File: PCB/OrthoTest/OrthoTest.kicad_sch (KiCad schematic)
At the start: 121 parts, among them SW1 SW_Push, SW10 SW_Push, SW11 SW_Push, SW12 SW_Push, SW13 SW_Push, SW14 SW_Push, SW15 SW_Push, SW16 SW_Push, SW17 SW_Push, SW18 SW_Push, SW19 SW_Push, SW2 SW_Push, SW20 SW_Push, SW21 SW_Push, SW22 SW_Push, SW23 SW_Push, SW24 SW_Push, SW25 SW_Push, SW26 SW_Push, SW27 SW_Push, SW28 SW_Push, SW29 SW_Push, SW3 SW_Push, SW30 SW_Push, SW31 SW_Push, SW32 SW_Push, SW33 SW_Push, SW34 SW_Push, SW35 SW_Push, SW36 SW_Push, SW37 SW_Push, SW38 SW_Push, SW39 SW_Push, SW4 SW_Push, SW40 SW_Push, SW41 SW_Push, SW42 SW_Push, SW43 SW_Push, SW44 SW_Push, SW45 SW_Push, SW46 SW_Push, SW47 SW_Push, SW48 SW_Push, SW49 SW_Push, SW5 SW_Push, SW50 SW_Push, SW51 SW_Push, SW52 SW_Push, SW53 SW_Push, SW54 SW_Push, SW55 SW_Push, SW56 SW_Push, SW57 SW_Push, SW58 SW_Push, SW59 SW_Push, SW6 SW_Push, SW60 SW_Push, SW7 SW_Push, SW8 SW_Push, SW9 SW_Push

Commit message: worked on it a lil
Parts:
- removed SW60: SW_Push, MyKeebLib:SW_Redragon_LowProfile_PCB_1.00u, symbol Switch:SW_Push
- added S1: MX_stab, PCM_marbastlib-mx:STAB_MX_2u, symbol PCM_marbastlib-mx:MX_stab
- added SW60, SW61: RotaryEncoder_Switch_MP, Rotary_Encoder:RotaryEncoder_Alps_EC11E-Switch_Vertical_H20mm, symbol Device:RotaryEncoder_Switch_MP
- added U1: ~, MyKeebLib:SSD1306-0.91-OLED-4pin-128x32, symbol MySymbols:ssd1306
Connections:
- net row1: now reaches D13.1 (K), D14.1 (K), D15.1 (K), D16.1 (K), D17.1 (K), D18.1 (K), D19.1 (K), D20.1 (K), D21.1 (K), D22.1 (K), D23.1 (K), D24.1 (K)
- net row2: now reaches D25.1 (K), D26.1 (K), D27.1 (K), D28.1 (K), D29.1 (K), D30.1 (K), D31.1 (K), D32.1 (K), D33.1 (K), D34.1 (K), D35.1 (K), D36.1 (K)
- net row0: now reaches D1.1 (K), D10.1 (K), D11.1 (K), D12.1 (K), D2.1 (K), D3.1 (K), D4.1 (K), D5.1 (K), D6.1 (K), D7.1 (K), D8.1 (K), D9.1 (K)
- net col10: now reaches SW47.1
- net col10: now also SW11.1, SW23.1, SW35.1, SW58.1
- net row3: now reaches D37.1 (K), D38.1 (K), D39.1 (K), D40.1 (K), D41.1 (K), D42.1 (K), D43.1 (K), D44.1 (K), D45.1 (K), D46.1 (K), D47.1 (K), D48.1 (K)
- net col2: now reaches SW3.1
- net col2: now also SW15.1, SW27.1, SW39.1, SW51.1
- net col0: now reaches SW25.1
- net col0: now also SW1.1, SW13.1, SW37.1, SW49.1
- net col7: now reaches SW8.1
- net col7: now also SW20.1, SW32.1, SW44.1, SW55.1
- net col1: now reaches SW50.1
- net col1: now also SW14.1, SW2.1, SW26.1, SW38.1
- net col5: now reaches SW30.1
- net col5: now also SW18.1, SW42.1, SW54.1, SW6.1
- net col4: now reaches SW41.1
- net col4: now also SW17.1, SW29.1, SW5.1, SW53.1
- net row4: now reaches D49.1 (K), D50.1 (K), D51.1 (K), D52.1 (K), D53.1 (K), D54.1 (K), D55.1 (K), D56.1 (K), D57.1 (K), D58.1 (K), D59.1 (K)
- net row4: no longer D60.1 (K)
- net col3: now reaches SW52.1
- net col3: now also SW16.1, SW28.1, SW4.1, SW40.1
- net col9: now reaches SW22.1
- net col9: now also SW10.1, SW34.1, SW46.1, SW57.1
- net col11: now reaches SW24.1
- net col11: now also SW12.1, SW36.1, SW48.1, SW59.1
- net col8: now reaches SW21.1
- net col8: now also SW33.1, SW45.1, SW56.1, SW9.1
- net col6: now reaches SW19.1
- net col6: now also SW31.1, SW43.1, SW7.1
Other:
- note added: "2U key (spacebar)"
- note added: "TODO add a switch from rotary encoder !!!! and diode for it"
- moved on the sheet: D1, D10, D11, D12, D13, D14, D15, D16, D17, D18, D19, D2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

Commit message: worked a lil on it
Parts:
- added A1: RaspberryPi_Pico, Module:RaspberryPi_Pico_Common_SMD, symbol MCU_Module:RaspberryPi_Pico
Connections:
- new net: A1.13 (GND), A1.18 (GND), A1.23 (GND), A1.28 (GND), A1.3 (GND), A1.38 (GND), A1.8 (GND)
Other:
- moved on the sheet: U1
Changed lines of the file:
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@@
 	(symbol
 		(lib_id "MySymbols:ssd1306")
-		(at 151.13 189.23 0)
+		(at 265.43 172.72 0)
 		(unit 1)
 		(exclude_from_sim no)
@@
 		(dnp no)
 		(property "Reference" "U1"
-			(at 151.13 188.722 0)
+			(at 265.43 172.212 0)
 			(effects
 				(font
@@
 		)
 		(property "Value" "~"
-			(at 152.4 189.23 0)
+			(at 266.7 172.72 0)
 			(effects
 				(font
@@
 		)
 		(property "Footprint" "MyKeebLib:SSD1306-0.91-OLED-4pin-128x32"
-			(at 151.13 189.23 0)
+			(at 265.43 172.72 0)
 			(effects
 				(font
@@
 		)
 		(property "Datasheet" ""
-			(at 151.13 189.23 0)
+			(at 265.43 172.72 0)
 			(effects
 				(font
@@
 		)
 		(property "Description" ""
-			(at 151.13 189.23 0)
+			(at 265.43 172.72 0)
 			(effects
 				(font
@@
 					(unit 1)
 				)
+			)
+		)
+	)
+	(symbol
+		(lib_id "MCU_Module:RaspberryPi_Pico")
+		(at 267.97 229.87 0)
+		(unit 1)
+		(exclude_from_sim no)
+		(in_bom yes)
+		(on_board yes)
+		(dnp no)
+		(fields_autoplaced yes)
+		(property "Reference" "A1"
+			(at 270.1133 264.16 0)
+			(effects
+				(font
+					(size 1.27 1.27)
+				)
+				(justify left)
+			)
+		)
+		(property "Value" "RaspberryPi_Pico"
+			(at 270.1133 266.7 0)
+			(effects
+				(font
+					(size 1.27 1.27)
+				)
+				(justify left)
+			)
+		)
+		(property "Footprint" "Module:RaspberryPi_Pico_Common_SMD"
+			(at 267.97 276.86 0)
+			(effects
+				(font
+					(size 1.27 1.27)
+				)
+				(hide yes)
+			)
+		)
+		(property "Datasheet" "https://datasheets.raspberrypi.com/pico/pico-datasheet.pdf"
+			(at 267.97 279.4 0)
+			(effects
+				(font
+					(size 1.27 1.27)
+				)
+				(hide yes)
+			)
+		)
+		(property "Description" "Versatile and inexpensive microcontroller module powered by RP2040 dual-core Arm Cortex-M0+ processor up to 133 MHz, 264kB SRAM, 2MB QSPI flash; also supports Raspberry Pi Pico 2"
+			(at 267.97 281.94 0)
+			(effects
+				(font
+					(size 1.27 1.27)
+				)
+				(hide yes)
+			)
+		)
+		(pin "37"
+		)
+		(pin "17"
+		)
+		(pin "19"
+		)
+		(pin "30"
+		)
+		(pin "1"
+		)
+		(pin "2"
+		)
+		(pin "4"
+		)
+		(pin "5"
+		)
+		(pin "6"
+		)
+		(pin "10"
+		)
+		(pin "9"
+		)
+		(pin "11"
+		)
+		(pin "14"
+		)
+		(pin "15"
+		)
+		(pin "7"
+		)
+		(pin "12"
+		)
+		(pin "16"
+		)
+		(pin "22"
+		)
+		(pin "23"
+		)
+		(pin "28"
+		)
+		(pin "38"
+		)
+		(pin "24"
+		)
+		(pin "31"
+		)
+		(pin "8"
+		)
+		(pin "20"
+		)
+		(pin "25"
+		)
+		(pin "13"
+		)
+		(pin "39"
+		)
+		(pin "18"
+		)
+		(pin "27"
+		)
+		(pin "21"
+		)
+		(pin "35"
+		)
+		(pin "40"
+		)
+		(pin "34"
+		)
+		(pin "36"
+		)
+		(pin "33"
+		)
+		(pin "3"
+		)
+		(pin "26"
+		)
+		(pin "32"
+		)
+		(pin "29"
+		)
+		(instances
+			(project ""
+				(path "/63f5a0a7-4058-42ed-a215-6578acb070e1"
+					(reference "A1")
+					(unit 1)
+				)

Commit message: done little work, not enought energy today :(
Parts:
- removed D60: D, MyKeebLib:D_SOD-123_SmallArrow, symbol Device:D
- added LED10, LED11, LED12, LED13, LED14, LED15, LED16, LED17, LED18, LED19, LED2, LED20, LED21, LED22, LED23, LED24, LED25, LED26, LED27, LED28, LED29, LED3, LED30, LED31, LED32, LED33, LED34, LED35, LED36, LED37, LED38, LED39, LED4, LED40, LED41, LED42, LED43, LED44, LED45, LED46, LED47, LED48, LED49, LED5, LED50, LED51, LED52, LED53, LED54, LED55, LED56, LED57, LED58, LED59, LED6, LED7, LED8, LED9: SK6812MINI-E, PCM_marbastlib-various:LED_6028R, symbol PCM_marbastlib-various:SK6812MINI-E
- LED1: footprint LED_SMD:LED_SK6812MINI_PLCC4_3.5x3.5mm_P1.75mm -> PCM_marbastlib-various:LED_6028R
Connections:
- net GND: now reaches SW61.C
- net GND: now also LED1.4 (VSS), SW60.C, U1.1 (GND), LED10.4 (VSS), LED11.4 (VSS), LED12.4 (VSS), LED13.4 (VSS), LED14.4 (VSS), LED15.4 (VSS), LED16.4 (VSS), LED17.4 (VSS), LED18.4 (VSS), LED19.4 (VSS), LED2.4 (VSS), LED20.4 (VSS), LED21.4 (VSS), LED22.4 (VSS), LED23.4 (VSS), LED24.4 (VSS), LED25.4 (VSS), LED26.4 (VSS), LED27.4 (VSS), LED28.4 (VSS), LED29.4 (VSS), LED3.4 (VSS), LED30.4 (VSS), LED31.4 (VSS), LED32.4 (VSS), LED33.4 (VSS), LED34.4 (VSS), LED35.4 (VSS), LED36.4 (VSS), LED37.4 (VSS), LED38.4 (VSS), LED39.4 (VSS), LED4.4 (VSS), LED40.4 (VSS), LED41.4 (VSS), LED42.4 (VSS), LED43.4 (VSS), LED44.4 (VSS), LED45.4 (VSS), LED46.4 (VSS), LED47.4 (VSS), LED48.4 (VSS), LED49.4 (VSS), LED5.4 (VSS), LED50.4 (VSS), LED51.4 (VSS), LED52.4 (VSS), LED53.4 (VSS), LED54.4 (VSS), LED55.4 (VSS), LED56.4 (VSS), LED57.4 (VSS), LED58.4 (VSS), LED59.4 (VSS), LED6.4 (VSS), LED7.4 (VSS), LED8.4 (VSS), LED9.4 (VSS)
- net +3V3: now reaches U1.2 (VCC)
- net oled_cl: now reaches U1.3 (SCL)
- net oled_data: now reaches U1.4 (SDA)
- net +5V: now reaches LED1.1 (VDD)
- net +5V: now also LED10.1 (VDD), LED11.1 (VDD), LED12.1 (VDD), LED13.1 (VDD), LED14.1 (VDD), LED15.1 (VDD), LED16.1 (VDD), LED17.1 (VDD), LED18.1 (VDD), LED19.1 (VDD), LED2.1 (VDD), LED20.1 (VDD), LED21.1 (VDD), LED22.1 (VDD), LED23.1 (VDD), LED24.1 (VDD), LED25.1 (VDD), LED26.1 (VDD), LED27.1 (VDD), LED28.1 (VDD), LED29.1 (VDD), LED3.1 (VDD), LED30.1 (VDD), LED31.1 (VDD), LED32.1 (VDD), LED33.1 (VDD), LED34.1 (VDD), LED35.1 (VDD), LED36.1 (VDD), LED37.1 (VDD), LED38.1 (VDD), LED39.1 (VDD), LED4.1 (VDD), LED40.1 (VDD), LED41.1 (VDD), LED42.1 (VDD), LED43.1 (VDD), LED44.1 (VDD), LED45.1 (VDD), LED46.1 (VDD), LED47.1 (VDD), LED48.1 (VDD), LED49.1 (VDD), LED5.1 (VDD), LED50.1 (VDD), LED51.1 (VDD), LED52.1 (VDD), LED53.1 (VDD), LED54.1 (VDD), LED55.1 (VDD), LED56.1 (VDD), LED57.1 (VDD), LED58.1 (VDD), LED59.1 (VDD), LED6.1 (VDD), LED7.1 (VDD), LED8.1 (VDD), LED9.1 (VDD)
- net at LED1.2 (DOUT): now also LED2.3 (DIN)
- net led_data: now reaches LED1.3 (DIN)
- new net: LED56.2 (DOUT), LED57.3 (DIN)
- new net: LED55.2 (DOUT), LED56.3 (DIN)
- new net: LED21.2 (DOUT), LED22.3 (DIN)
- new net: LED20.2 (DOUT), LED21.3 (DIN)
- new net: LED18.2 (DOUT), LED19.3 (DIN)
- new net: LED17.2 (DOUT), LED18.3 (DIN)
- new net: LED10.3 (DIN), LED9.2 (DOUT)
- new net: LED8.2 (DOUT), LED9.3 (DIN)
- new net: LED53.2 (DOUT), LED54.3 (DIN)
- new net: LED52.2 (DOUT), LED53.3 (DIN)
- new net: LED54.2 (DOUT), LED55.3 (DIN)
- new net: LED15.2 (DOUT), LED16.3 (DIN)
- new net: LED14.2 (DOUT), LED15.3 (DIN)
- new net: LED36.2 (DOUT), LED37.3 (DIN)
- new net: LED35.2 (DOUT), LED36.3 (DIN)
- new net: LED6.2 (DOUT), LED7.3 (DIN)
- new net: LED5.2 (DOUT), LED6.3 (DIN)
- new net: LED47.2 (DOUT), LED48.3 (DIN)
- new net: LED46.2 (DOUT), LED47.3 (DIN)
- new net: LED7.2 (DOUT), LED8.3 (DIN)
- new net: LED49.2 (DOUT), LED50.3 (DIN)
- new net: LED48.2 (DOUT), LED49.3 (DIN)
- new net: LED45.2 (DOUT), LED46.3 (DIN)
- new net: LED44.2 (DOUT), LED45.3 (DIN)
- new net: LED31.2 (DOUT), LED32.3 (DIN)
- new net: LED30.2 (DOUT), LED31.3 (DIN)
- new net: LED32.2 (DOUT), LED33.3 (DIN)
- new net: LED27.2 (DOUT), LED28.3 (DIN)
- new net: LED26.2 (DOUT), LED27.3 (DIN)
- new net: LED3.2 (DOUT), LED4.3 (DIN)
- new net: LED2.2 (DOUT), LED3.3 (DIN)
- new net: LED19.2 (DOUT), LED20.3 (DIN)
- new net: LED23.2 (DOUT), LED24.3 (DIN)
- new net: LED22.2 (DOUT), LED23.3 (DIN)
- new net: LED42.2 (DOUT), LED43.3 (DIN)
- new net: LED41.2 (DOUT), LED42.3 (DIN)
- new net: LED43.2 (DOUT), LED44.3 (DIN)
- new net: LED39.2 (DOUT), LED40.3 (DIN)
- new net: LED38.2 (DOUT), LED39.3 (DIN)
- new net: LED11.2 (DOUT), LED12.3 (DIN)
- new net: LED10.2 (DOUT), LED11.3 (DIN)
- new net: LED50.2 (DOUT), LED51.3 (DIN)
- new net: LED25.2 (DOUT), LED26.3 (DIN)
- new net: LED51.2 (DOUT), LED52.3 (DIN)
- new net: LED16.2 (DOUT), LED17.3 (DIN)
- new net: LED57.2 (DOUT), LED58.3 (DIN)
- new net: LED34.2 (DOUT), LED35.3 (DIN)
- new net: LED28.2 (DOUT), LED29.3 (DIN)
- new net: LED4.2 (DOUT), LED5.3 (DIN)
- new net: LED37.2 (DOUT), LED38.3 (DIN)
- new net: LED13.2 (DOUT), LED14.3 (DIN)
- new net: LED24.2 (DOUT), LED25.3 (DIN)
- new net: LED29.2 (DOUT), LED30.3 (DIN)
- new net: LED58.2 (DOUT), LED59.3 (DIN)
- new net: LED40.2 (DOUT), LED41.3 (DIN)
- new net: LED12.2 (DOUT), LED13.3 (DIN)
- new net: LED33.2 (DOUT), LED34.3 (DIN)
- no-connect marks 0 -> 1
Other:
- moved on the sheet: A1, SW60, SW61, U1

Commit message: added libraries and placed pcb components
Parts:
- renumbered S1 to S54
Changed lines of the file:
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@@
 			"ZogUyS0cwZsxsCbqBwcIiDYM4ph6zEmRItYD3ZiOo73PS4SIPUEKGHxRaq+V5T02UtQVLIDAQkqA"
 			"yCiqosVvGAnIxlHbS8/rr4KmqjSt6UfpGAUzm6sMIphkRVHZ5jWgKiE4BIdKNnxMbe4YJJRhmg79"
-			"ANpkh8qgAWJtN7S4838BfKgryf/pyQkAAAAASUVORK5CYII="
+			"ANpkh8qgAWJtN7S4838BfKgryf/pyQkAAAAASUVORK5CYIIAAAAAAAAAAAAAAAAAAAAAAAAAAAAA"
+			"AAAAAAAAAAAAAAAAAAAAAAAAAAAAAAAAAAAAAAAAAAAAAAAAAAAAAAAAAAAAAAAAAAAAAAAAAAAA"
+			"AAAAAAAAAAAAAAAAAAAAAAAAAAAAAAAAAAAAAAAAAAAAAAAAAAAAAAAAAAAAAAAAAAAAAAAAAAAA"
+			"AAAAAAAAAAAAAAAAAAAAAAAAAAAAAAAAAAAAAAAAAAAAAAAAAAAAAAAAAAAAAAAAAAAAAAAAAAAA"
+			"AAAAAAAAAAAAAAAAAAAAAAAAAAAAAAAAAAAAAAAAAAAAAAAAAAAAAAAAAAAAAAAAAAAAAAAAAAAA"
+			"AAAAAAAAAAAAAAAAAAAAAAAAAAAAAAAAAAAAAAAAAAAAAAAAAAAAAAAAAAAAAAAAAAAAAAAAAAAA"
+			"AAAAAAAAAAAAAAAAAAAAAAAAAAAAAAAAAAAAAAAAAAAAAAAAAAAAAAAAAAAAAAAAAAAAAAAAAAAA"
+			"AAAAAAAAAAAAAAAAAAAAAAAAAAAAAAAAAAAAAAAAAAAAAAAAAAAAAAAAAAAAAAAAAAAAAAAAAAAA"
+			"AAAAAAAAAAAAAAAAAAAAAAAAAAAAAAAAAAAAAAAAAAAAAAAAAAAAAAAAAAAAAAAAAAAAAAAAAAAA"
+			"AAAAAAAAAAAAAAAAAAAAAAAAAAAAAAAAAAAAAAAAAAAAAAAAAAAAAAAAAAAAAAAAAAAAAAAAAAAA"
+			"AAAAAAAAAAAAAAAAAAAAAAAAAAAAAAAAAAAAAAAAAAAAAAAAAAAAAAAAAAAAAAAAAAAAAAAAAAAA"
+			"AAAAAAAAAAAAAAAAAAAAAAAAAAAAAAAAAAAAAAAAAAAAAAAAAAAAAAAAAAAAAAAAAAAAAAAAAAAA"
+			"AAAAAAAAAAAAAAAAAAAAAAAAAAAAAAAAAAAAAAAAAAAAAAAAAAAAAAAAAAAAAAAAAAAAAAAAAAAA"
+			"AAAAAAAAAAAAAAAAAAAAAAAAAAAAAAAAAAAAAAAAAAAAAAAAAAAAAAAAAAAAAAAAAAAAAAAAAAAA"
+			"AAAAAAAAAAAAAAAAAAAAAAAAAAAAAAAAAAAAAAAAAAAAAAAAAAAAAAAAAAAAAAAAAAAAAAAAAAAA"
+			"AAAAAAAAAAAAAAAAAAAAAAAAAAAAAAAAAAAAAAAAAAAAAAAAAAAAAAAAAAAAAAAAAAAAAAAAAAAA"
+			"AAAAAAAAAAAAAAAAAAAAAAAAAAAAAAAAAAAAAAAAAAAAAAAAAAAAAAAAAAAAAAAAAAAAAAAAAAAA"
+			"AAAAAAAAAAAAAAAAAAAAAAAAAAAAAAAAAAAAAAAAAAAAAAAAAAAAAAAAAAAAAAAAAAAAAAAAAAAA"
+			"AAAAAAAAAAAAAAAAAAAAAAAAAAAAAAAAAAAAAAAAAAAAAA=="
 		)
 	)
@@
 		(dnp no)
 		(fields_autoplaced yes)
-		(property "Reference" "S1"
+		(property "Reference" "S54"
 			(at 133.35 143.3829 0)
 			(effects
@@
 			(project ""
 				(path "/63f5a0a7-4058-42ed-a215-6578acb070e1"
-					(reference "S1")
+					(reference "S54")
 					(unit 1)
 				)

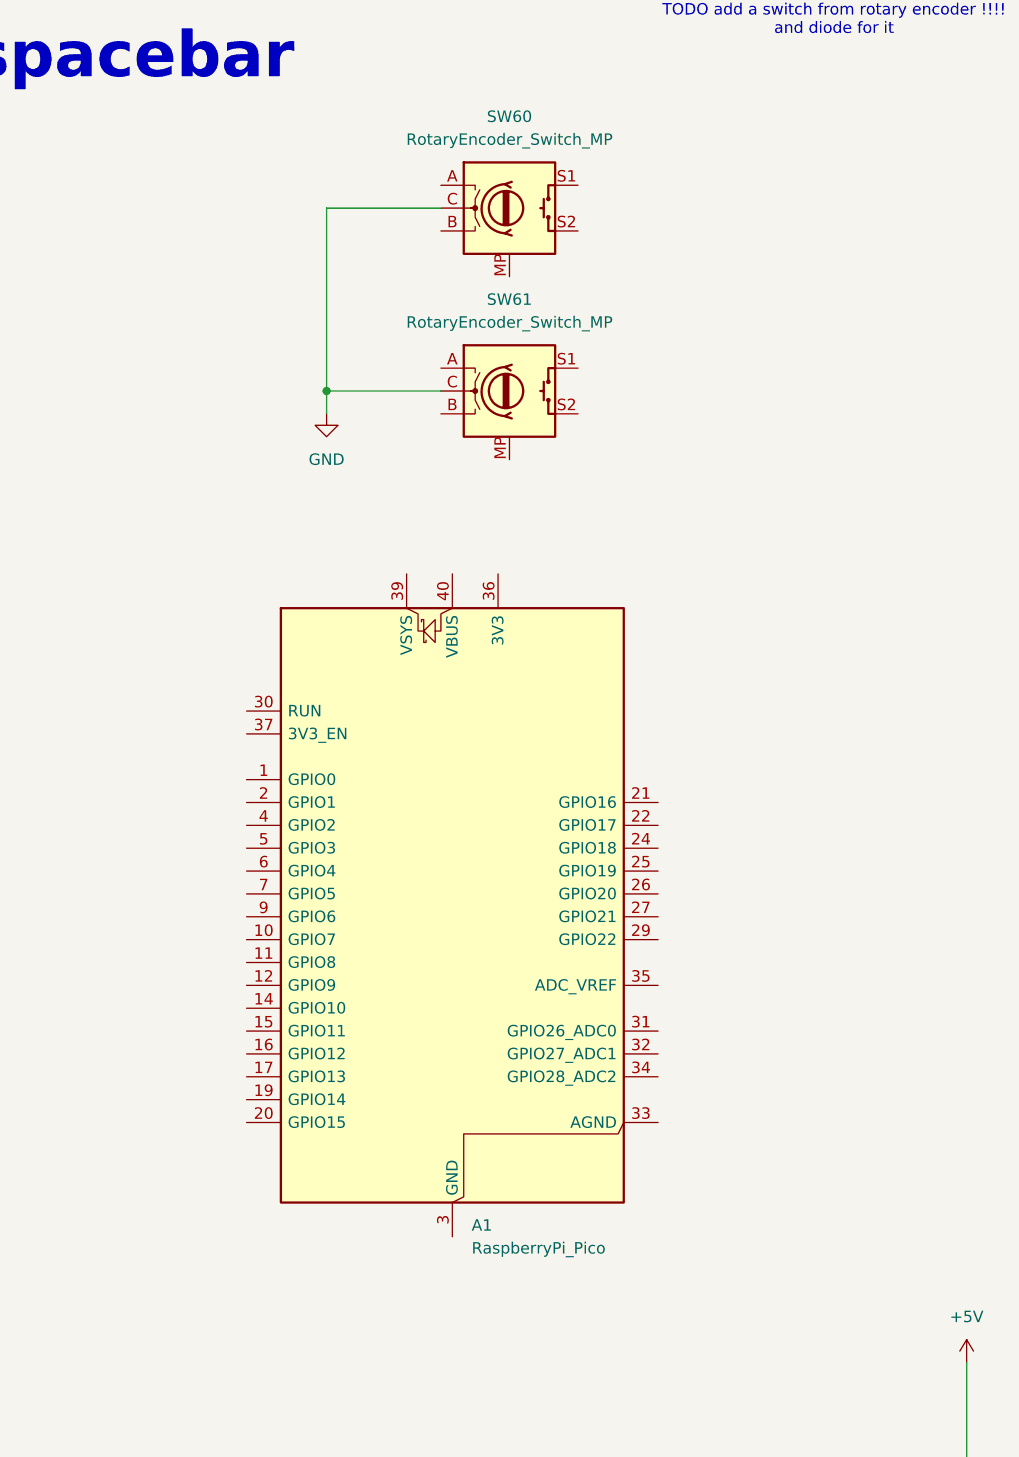
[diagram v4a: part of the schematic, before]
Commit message: finished routing pcb
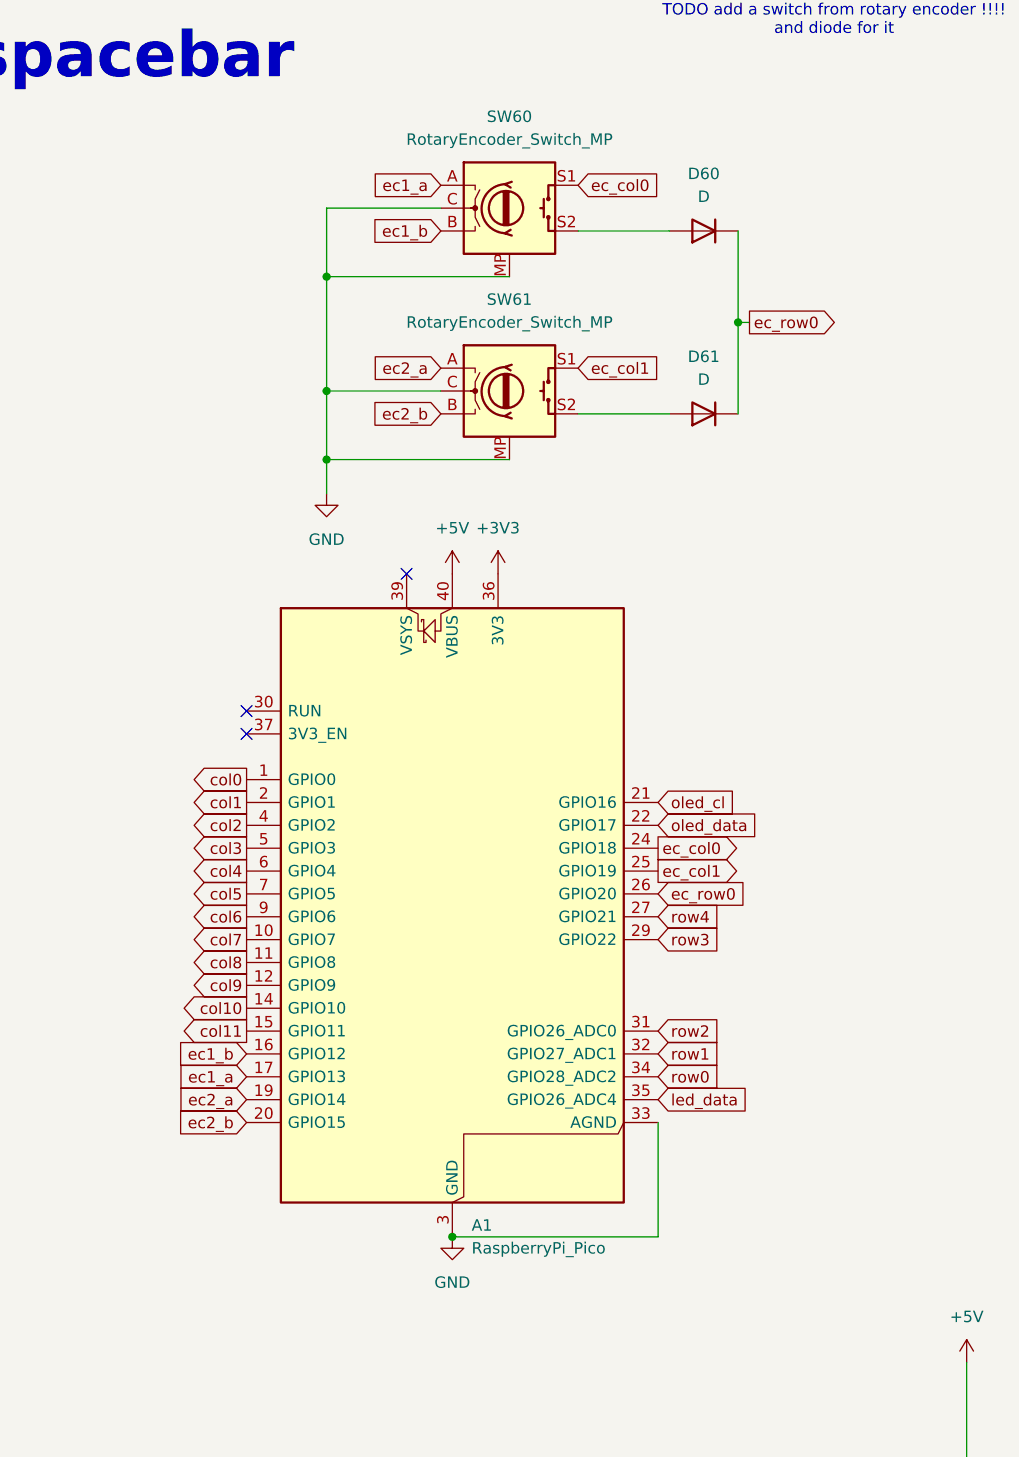
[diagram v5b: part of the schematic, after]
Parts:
- added D60, D61: D, MyKeebLib:D_SOD-123_SmallArrow, symbol Device:D
- A1: footprint Module:RaspberryPi_Pico_Common_SMD -> Module:RaspberryPi_Pico_Common_THT
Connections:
- net +3V3: now also A1.36 (3V3)
- net +5V: now also A1.40 (VBUS)
- net GND: now also A1.13 (GND), A1.18 (GND), A1.23 (GND), A1.28 (GND), A1.3 (GND), A1.33 (AGND), A1.38 (GND), A1.8 (GND), SW60.MP, SW61.MP
- net col0: now also A1.1 (GPIO0)
- net col1: now also A1.2 (GPIO1)
- net col10: now also A1.14 (GPIO10)
- net col11: now also A1.15 (GPIO11)
- net col2: now also A1.4 (GPIO2)
- net col3: now also A1.5 (GPIO3)
- net col4: now also A1.6 (GPIO4)
- net col5: now also A1.7 (GPIO5)
- net col6: now also A1.9 (GPIO6)
- net col7: now also A1.10 (GPIO7)
- net col8: now also A1.11 (GPIO8)
- net col9: now also A1.12 (GPIO9)
- net led_data: now also A1.35 (GPIO26_ADC4)
- net oled_cl: now also A1.21 (GPIO16)
- net oled_data: now also A1.22 (GPIO17)
- net row0: now also A1.34 (GPIO28_ADC2)
- net row1: now also A1.32 (GPIO27_ADC1)
- net row2: now also A1.31 (GPIO26_ADC0)
- net row3: now also A1.29 (GPIO22)
- net row4: now also A1.27 (GPIO21)
- net ec2_a: now reaches SW61.A
- net ec2_a: now also A1.19 (GPIO14)
- net ec2_b: now reaches SW61.B
- net ec2_b: now also A1.20 (GPIO15)
- net ec_col1: now reaches SW61.S1
- net ec_col1: now also A1.25 (GPIO19)
- net at SW61.S2: now also D61.2 (A)
- net ec1_b: now reaches A1.16 (GPIO12)
- net ec1_b: now also SW60.B
- net ec1_a: now reaches A1.17 (GPIO13)
- net ec1_a: now also SW60.A
- net ec_col0: now reaches A1.24 (GPIO18)
- net ec_col0: now also SW60.S1
- net ec_row0: now reaches A1.26 (GPIO20)
- net ec_row0: now also D60.1 (K), D61.1 (K)
- net at SW60.S2: now also D60.2 (A)
- no-connect marks 1 -> 4

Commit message: fixed ucontroller usb c position and added grounding vias
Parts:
- added C1, C10, C11, C12, C13, C14, C15, C16, C17, C18, C19, C2, C20, C21, C22, C23, C24, C25, C26, C27, C28, C29, C3, C30, C31, C32, C33, C34, C35, C36, C37, C38, C39, C4, C40, C41, C42, C43, C44, C45, C46, C47, C48, C49, C5, C50, C51, C52, C53, C54, C55, C56, C57, C58, C59, C6, C7, C8, C9: 100n, Capacitor_SMD:C_0603_1608Metric, symbol Device:C
- added H1, H2, H3, H4, H5, H6: MountingHolePlate, MyKeebLib:Spacer_3.2mm, symbol Mechanical:MountingHole
- SW60, SW61: LCSC C202365 -> (none); TME (none) -> https://www.tme.eu/cz/details/ec11e15244b2/inkrementalni-en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
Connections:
- net +5V: now also C1.1, C10.1, C11.1, C12.1, C13.1, C14.1, C15.1, C16.1, C17.1, C18.1, C19.1, C2.1, C20.1, C21.1, C22.1, C23.1, C24.1, C25.1, C26.1, C27.1, C28.1, C29.1, C3.1, C30.1, C31.1, C32.1, C33.1, C34.1, C35.1, C36.1, C37.1, C38.1, C39.1, C4.1, C40.1, C41.1, C42.1, C43.1, C44.1, C45.1, C46.1, C47.1, C48.1, C49.1, C5.1, C50.1, C51.1, C52.1, C53.1, C54.1, C55.1, C56.1, C57.1, C58.1, C59.1, C6.1, C7.1, C8.1, C9.1
- net GND: now also C1.2, C10.2, C11.2, C12.2, C13.2, C14.2, C15.2, C16.2, C17.2, C18.2, C19.2, C2.2, C20.2, C21.2, C22.2, C23.2, C24.2, C25.2, C26.2, C27.2, C28.2, C29.2, C3.2, C30.2, C31.2, C32.2, C33.2, C34.2, C35.2, C36.2, C37.2, C38.2, C39.2, C4.2, C40.2, C41.2, C42.2, C43.2, C44.2, C45.2, C46.2, C47.2, C48.2, C49.2, C5.2, C50.2, C51.2, C52.2, C53.2, C54.2, C55.2, C56.2, C57.2, C58.2, C59.2, C6.2, C7.2, C8.2, C9.2
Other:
- note added: "Hardware"
- note added: "LED bank"
- note added: "LED capacitor bank"
- note added: "OLED display"
- note added: "Rotary encoders"
- note added: "Switch matrix"
- note added: "uController"
- note removed: "TODO add a switch from rotary encoder !!!! and diode for it"
- moved on the sheet: A1, D60, D61, SW60, SW61, U1
